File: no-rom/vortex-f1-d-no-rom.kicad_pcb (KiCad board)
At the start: 2 copper layers, 111.9 x 64.1 mm, 47 parts, among them IC1 74LS136, IC10 uPD765AC, IC11 74HCT688, IC12 74LS38, IC13 74LS07, IC14 74LS139, IC15 74HCT688, IC2 74LS74, IC5 74LS14, IC6 74LS08, IC7 74HCT688, IC8 74LS32, IC9 FDC_9229, X1 8Mhz

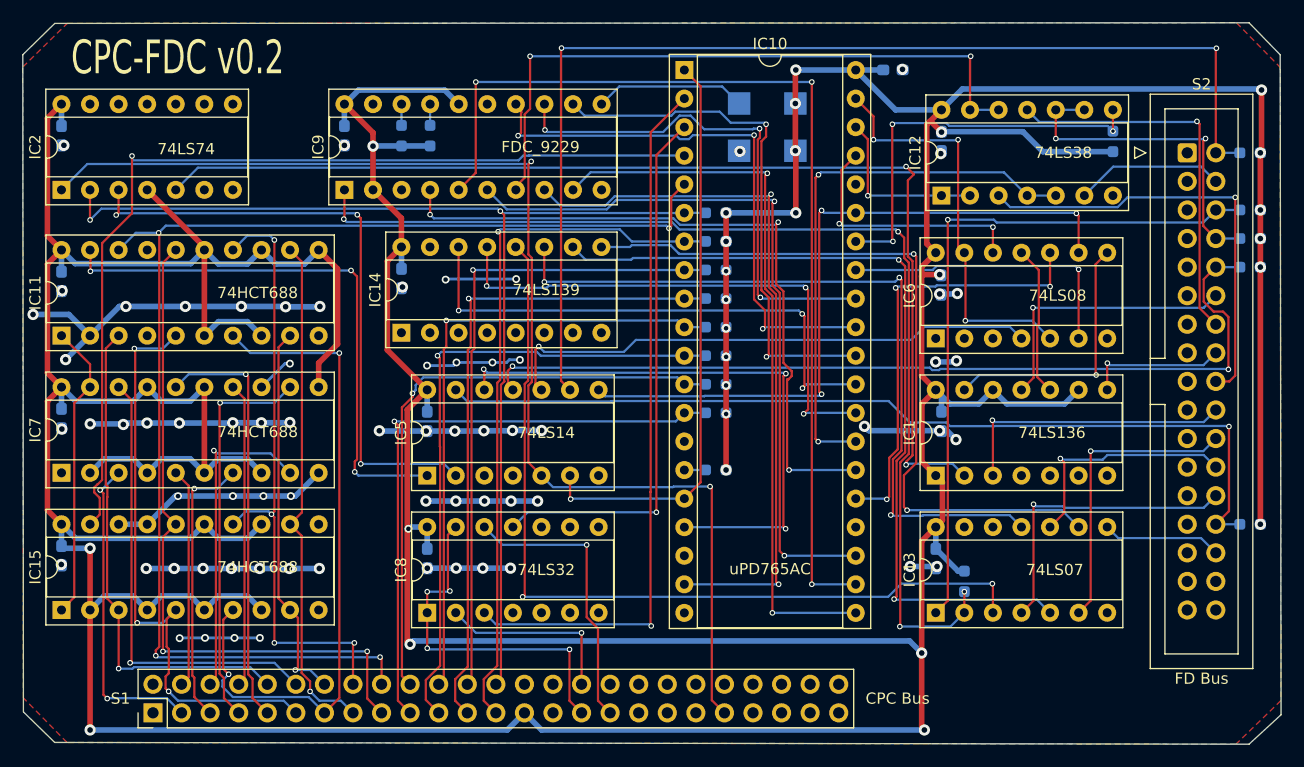
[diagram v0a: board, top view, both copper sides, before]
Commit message: reorganize and fix no-rom pcb and schematic
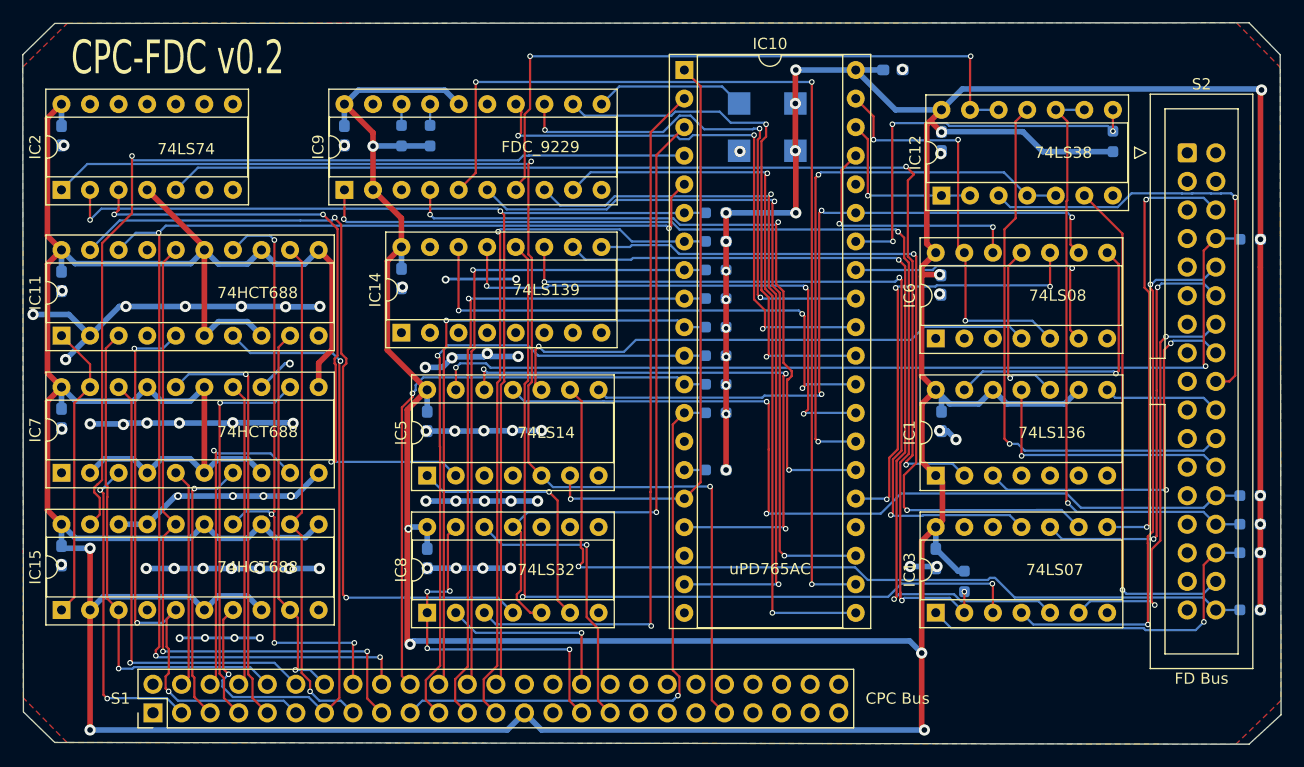
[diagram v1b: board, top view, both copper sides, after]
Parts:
- moved R13 40.6 mm to (200.0, 120.2)
- moved R20 30.5 mm to (200.0, 115.1)
- moved R2 25.4 mm to (200.0, 112.6)
- moved R3 25.3 mm to (200.0, 87.3)
- moved R1 20.3 mm to (200.0, 110.1)
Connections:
- IC15 pad 11: GND -> +5V
- IC15 pad 4: +5V -> GND
- IC5 pad 1: ~{MOTCS} -> Net-(IC5-Pad1)
- IC8 pad 4: (no net) -> ~{MOTCS}
- IC8 pad 5: (no net) -> ~{IOWR}
- IC8 pad 6: (no net) -> Net-(IC5-Pad1)
- S2 pad 10: ~{TRK00} -> ~{DS0}
- S2 pad 12: ~{WGATE} -> ~{DS1}
- S2 pad 14: ~{WDATA} -> ~{DS2}
- S2 pad 16: ~{STEP} -> ~{MTRON}
- S2 pad 2: ~{RDY} -> unconnected-(S2-Pad2)
- S2 pad 20: ~{MTRON} -> ~{STEP}
- S2 pad 22: ~{DS2} -> ~{WDATA}
- S2 pad 24: ~{DS1} -> ~{WGATE}
- S2 pad 26: ~{DS0} -> ~{TRK00}
- S2 pad 28: ~{INDEX} -> ~{WPT}
- S2 pad 30: ~{DS3} -> ~{RDATA}
- S2 pad 32: unconnected-(S2-Pad32) -> ~{SIDE1}
- S2 pad 34: unconnected-(S2-Pad34) -> ~{RDY}
- S2 pad 4: ~{SIDE1} -> unconnected-(S2-Pad4)
- S2 pad 6: ~{RDATA} -> ~{DS3}
- S2 pad 8: ~{WPT} -> ~{INDEX}
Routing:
- net ~{SIDE1}: track 13.3 -> 45.4 mm, vias 0 -> 1
- net ~{DS3}: track 10.6 -> 39.7 mm, vias 0 -> 2
- net ~{RDATA}: track 61.9 -> 33.5 mm
- net ~{WPT}: track 30.0 -> 54.1 mm, vias 2 -> 1
- net ~{RDY}: track 100.4 -> 77.0 mm, vias 2 -> 1
- net Net-(IC5-Pad1): track 0.00 -> 22.9 mm, vias 0 -> 1
- net ~{MOTCS}: track 49.9 -> 72.8 mm, vias 3 -> 2
- net ~{DS0}: track 26.9 -> 48.6 mm, vias 1 -> 2
- net ~{DS1}: track 21.2 -> 37.9 mm, vias 1 -> 2
- net ~{WDATA}: track 34.3 -> 49.7 mm
- net GND: track 156.3 -> 142.6 mm, vias 69 -> 63
- net +5V: track 634.0 -> 646.3 mm
- net ~{DS2}: track 26.4 -> 36.7 mm, vias 1 -> 2
- net ~{IOWR}: track 48.6 -> 58.3 mm
- net ~{MTRON}: track 25.3 -> 33.8 mm, vias 1 -> 2
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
